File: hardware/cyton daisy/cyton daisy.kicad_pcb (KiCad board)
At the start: 4 copper layers, 61.4 x 39.7 mm, 41 parts, among them J1 Conn_02x13_Odd_Even, J2 Conn_01x08, J4 Conn_01x02, U1 ADS129x

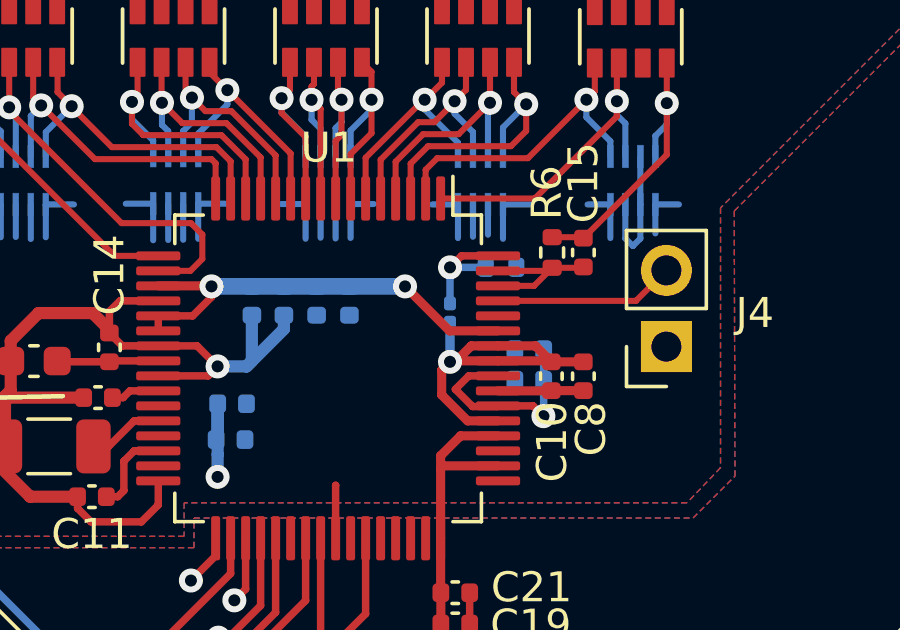
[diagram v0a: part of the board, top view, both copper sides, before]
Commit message: changed C27 from an 0402 package to a 0201 package
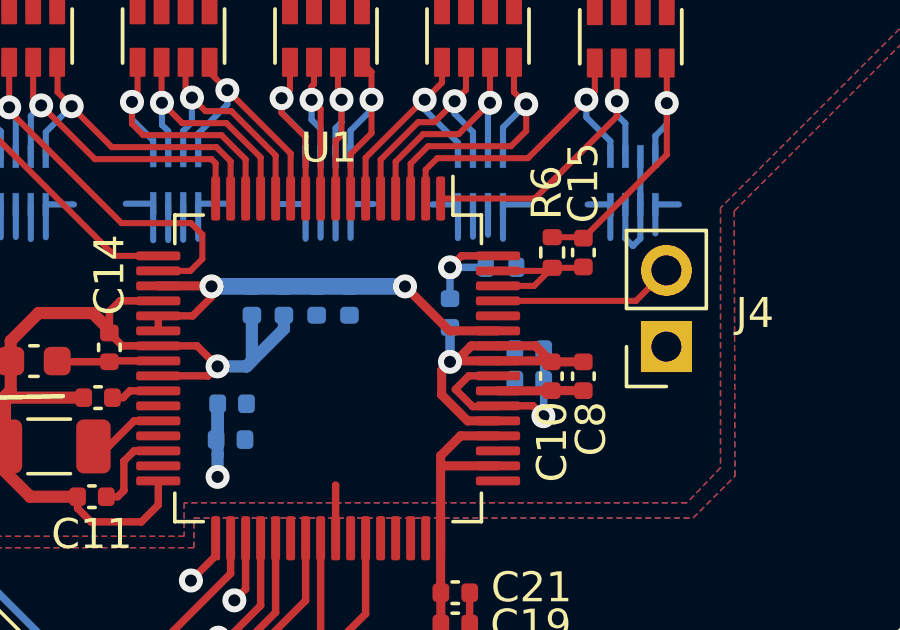
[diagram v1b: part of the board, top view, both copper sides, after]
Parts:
- C27: footprint Capacitor_SMD:C_0201_0603Metric -> Capacitor_SMD:C_0402_1005Metric
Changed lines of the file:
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@@
     )
   )
-  (footprint "Capacitor_SMD:C_0201_0603Metric" (layer "B.Cu")
+  (footprint "Capacitor_SMD:C_0402_1005Metric" (layer "B.Cu")
     (at 142.6972 100.0252 90)
-    (descr "Capacitor SMD 0201 (0603 Metric), square (rectangular) end terminal, IPC_7351 nominal, (Body size source: https://www.vishay.com/docs/20052/crcw0201e3.pdf), generated with kicad-footprint-generator")
+    (descr "Capacitor SMD 0402 (1005 Metric), square (rectangular) end terminal, IPC_7351 nominal, (Body size source: IPC-SM-782 page 76, https://www.pcb-3d.com/wordpress/wp-content/uploads/ipc-sm-782a_amendment_1_and_2.pdf), generated with kicad-footprint-generator")
     (tags "capacitor")
     (property "Sheetfile" "../shared schematics/ADS129X-X functionality.kicad_sch")
@@
     (property "ki_keywords" "cap capacitor")
     (attr smd)
-    (fp_text reference "C27" (at -2.159 0 90) (layer "B.SilkS")
-        (effects (font (size 1 1) (thickness 0.15)) (justify mirror))
-    )
-    (fp_text value "1nF" (at 0 -1.05 90) (layer "B.Fab")
-        (effects (font (size 1 1) (thickness 0.15)) (justify mirror))
-    )
-    (fp_text user "${REFERENCE}" (at 0 0.68 90) (layer "B.Fab")
+    (fp_text reference "C27" (at 0 1.16 270) (layer "B.SilkS")
+        (effects (font (size 1 1) (thickness 0.15)) (justify mirror))
+    )
+    (fp_text value "1nF" (at 0 -1.16 270) (layer "B.Fab")
+        (effects (font (size 1 1) (thickness 0.15)) (justify mirror))
+    )
+    (fp_text user "${REFERENCE}" (at 0 0 270) (layer "B.Fab")
         (effects (font (size 0.25 0.25) (thickness 0.04)) (justify mirror))
     )
-    (fp_line (start -0.7 -0.35) (end -0.7 0.35)
-      (stroke (width 0.05) (type solid)) (layer "B.CrtYd"))
-    (fp_line (start -0.7 0.35) (end 0.7 0.35)
-      (stroke (width 0.05) (type solid)) (layer "B.CrtYd"))
-    (fp_line (start 0.7 -0.35) (end -0.7 -0.35)
-      (stroke (width 0.05) (type solid)) (layer "B.CrtYd"))
-    (fp_line (start 0.7 0.35) (end 0.7 -0.35)
-      (stroke (width 0.05) (type solid)) (layer "B.CrtYd"))
-    (fp_line (start -0.3 -0.15) (end -0.3 0.15)
-      (stroke (width 0.1) (type solid)) (layer "B.Fab"))
-    (fp_line (start -0.3 0.15) (end 0.3 0.15)
-      (stroke (width 0.1) (type solid)) (layer "B.Fab"))
-    (fp_line (start 0.3 -0.15) (end -0.3 -0.15)
-      (stroke (width 0.1) (type solid)) (layer "B.Fab"))
-    (fp_line (start 0.3 0.15) (end 0.3 -0.15)
-      (stroke (width 0.1) (type solid)) (layer "B.Fab"))
-    (pad "" smd roundrect (at -0.345 0 90) (size 0.318 0.36) (layers "B.Paste") (roundrect_rratio 0.25))
-    (pad "" smd roundrect (at 0.345 0 90) (size 0.318 0.36) (layers "B.Paste") (roundrect_rratio 0.25))
-    (pad "1" smd roundrect (at -0.32 0 90) (size 0.46 0.4) (layers "B.Cu" "B.Mask") (roundrect_rratio 0.25)
+    (fp_line (start -0.107836 -0.36) (end 0.107836 -0.36)
+      (stroke (width 0.12) (type solid)) (layer "B.SilkS"))
+    (fp_line (start -0.107836 0.36) (end 0.107836 0.36)
+      (stroke (width 0.12) (type solid)) (layer "B.SilkS"))
+    (fp_line (start -0.91 -0.46) (end -0.91 0.46)
+      (stroke (width 0.05) (type solid)) (layer "B.CrtYd"))
+    (fp_line (start -0.91 0.46) (end 0.91 0.46)
+      (stroke (width 0.05) (type solid)) (layer "B.CrtYd"))
+    (fp_line (start 0.91 -0.46) (end -0.91 -0.46)
+      (stroke (width 0.05) (type solid)) (layer "B.CrtYd"))
+    (fp_line (start 0.91 0.46) (end 0.91 -0.46)
+      (stroke (width 0.05) (type solid)) (layer "B.CrtYd"))
+    (fp_line (start -0.5 -0.25) (end -0.5 0.25)
+      (stroke (width 0.1) (type solid)) (layer "B.Fab"))
+    (fp_line (start -0.5 0.25) (end 0.5 0.25)
+      (stroke (width 0.1) (type solid)) (layer "B.Fab"))
+    (fp_line (start 0.5 -0.25) (end -0.5 -0.25)
+      (stroke (width 0.1) (type solid)) (layer "B.Fab"))
+    (fp_line (start 0.5 0.25) (end 0.5 -0.25)
+      (stroke (width 0.1) (type solid)) (layer "B.Fab"))
+    (pad "1" smd roundrect (at -0.48 0 90) (size 0.56 0.62) (layers "B.Cu" "B.Paste" "B.Mask") (roundrect_rratio 0.25)
       (net 21 "VSSA") (pintype "passive"))
-    (pad "2" smd roundrect (at 0.32 0 90) (size 0.46 0.4) (layers "B.Cu" "B.Mask") (roundrect_rratio 0.25)
+    (pad "2" smd roundrect (at 0.48 0 90) (size 0.56 0.62) (layers "B.Cu" "B.Paste" "B.Mask") (roundrect_rratio 0.25)
       (net 31 "Net-(U1-WCT)") (pintype "passive"))
-    (model "${KICAD6_3DMODEL_DIR}/Capacitor_SMD.3dshapes/C_0201_0603Metric.wrl"
+    (model "${KICAD6_3DMODEL_DIR}/Capacitor_SMD.3dshapes/C_0402_1005Metric.wrl"
       (offset (xyz 0 0 0))
       (scale (xyz 1 1 1))
@@
   (via (at 134.9502 105.4862) (size 0.8) (drill 0.4) (layers "F.Cu" "B.Cu") (free) (net 21))
   (via (at 142.6972 101.6508) (size 0.8) (drill 0.4) (layers "F.Cu" "B.Cu") (net 21))
+  (segment (start 142.6972 101.6508) (end 142.6972 100.5052) (width 0.3048) (layer "B.Cu") (net 21))
   (segment (start 134.9502 105.4862) (end 134.9502 104.7424) (width 0.4064) (layer "B.Cu") (net 21))
   (segment (start 135.9154 101.8032) (end 137.16 100.5586) (width 0.4064) (layer "B.Cu") (net 21))
@@
   (segment (start 124.6632 87.63) (end 126.176799 89.143599) (width 0.2032) (layer "B.Cu") (net 21))
   (segment (start 134.9528 103.0478) (end 134.9528 104.1934) (width 0.4064) (layer "B.Cu") (net 21))
-  (segment (start 142.6972 101.6508) (end 142.6972 100.3452) (width 0.3048) (layer "B.Cu") (net 21))
   (segment (start 132.0264 102.6188) (end 132.9724 102.6188) (width 0.25) (layer "F.Cu") (net 22))
   (segment (start 131.8006 102.8446) (end 132.0264 102.6188) (width 0.25) (layer "F.Cu") (net 22))
@@
   (segment (start 143.0796 98.1188) (end 144.2974 98.1188) (width 0.25) (layer "F.Cu") (net 31))
   (via (at 142.6972 98.5012) (size 0.8) (drill 0.4) (layers "F.Cu" "B.Cu") (net 31))
+  (segment (start 142.6972 99.5452) (end 142.6972 98.5012) (width 0.25) (layer "B.Cu") (net 31))
   (segment (start 142.6972 98.5012) (end 143.889 98.5012) (width 0.25) (layer "B.Cu") (net 31))
-  (segment (start 142.6972 99.7052) (end 142.6972 98.5012) (width 0.25) (layer "B.Cu") (net 31))
   (segment (start 129.7432 84.9884) (end 129.7432 86.5886) (width 0.2032) (layer "F.Cu") (net 32))
   (segment (start 128.8032 87.5286) (end 128.8032 89.916) (width 0.2032) (layer "F.Cu") (net 32))

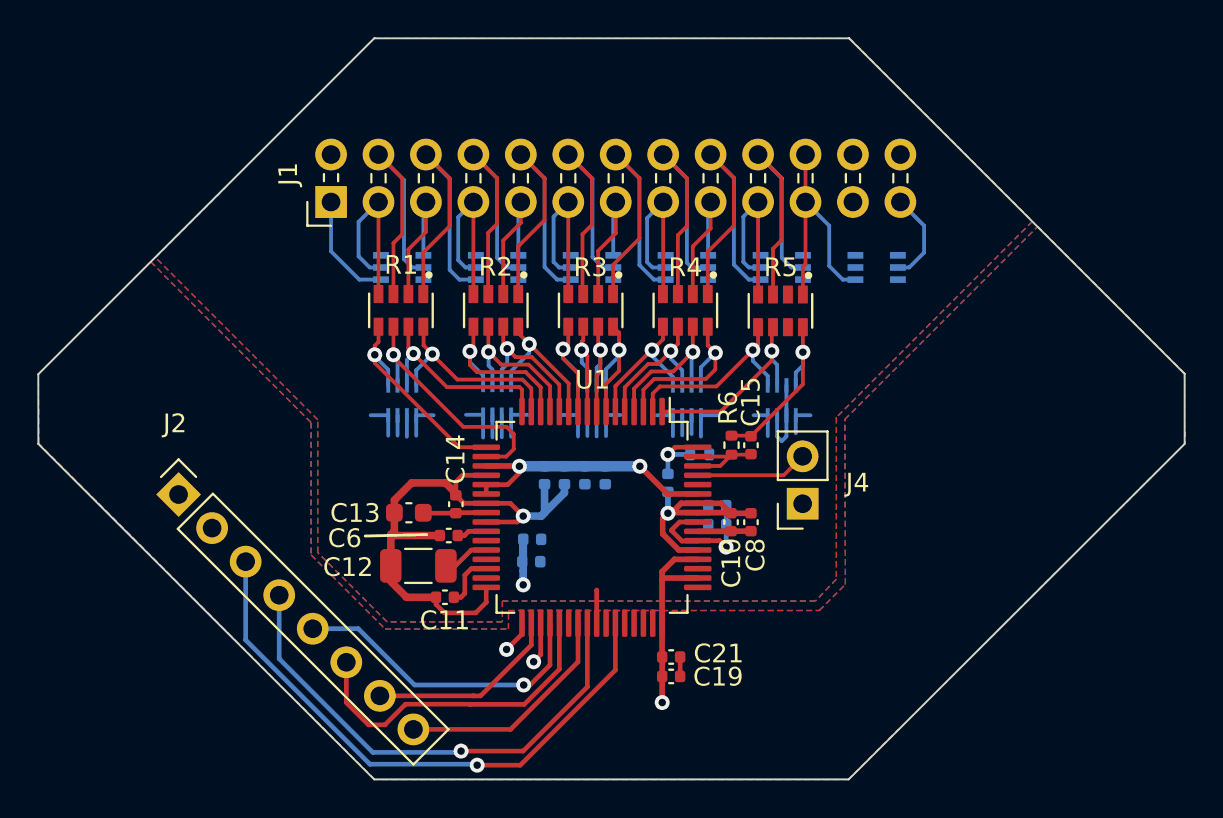
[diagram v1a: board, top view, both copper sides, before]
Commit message: changed C27 from an 0402 package to a 0201 package
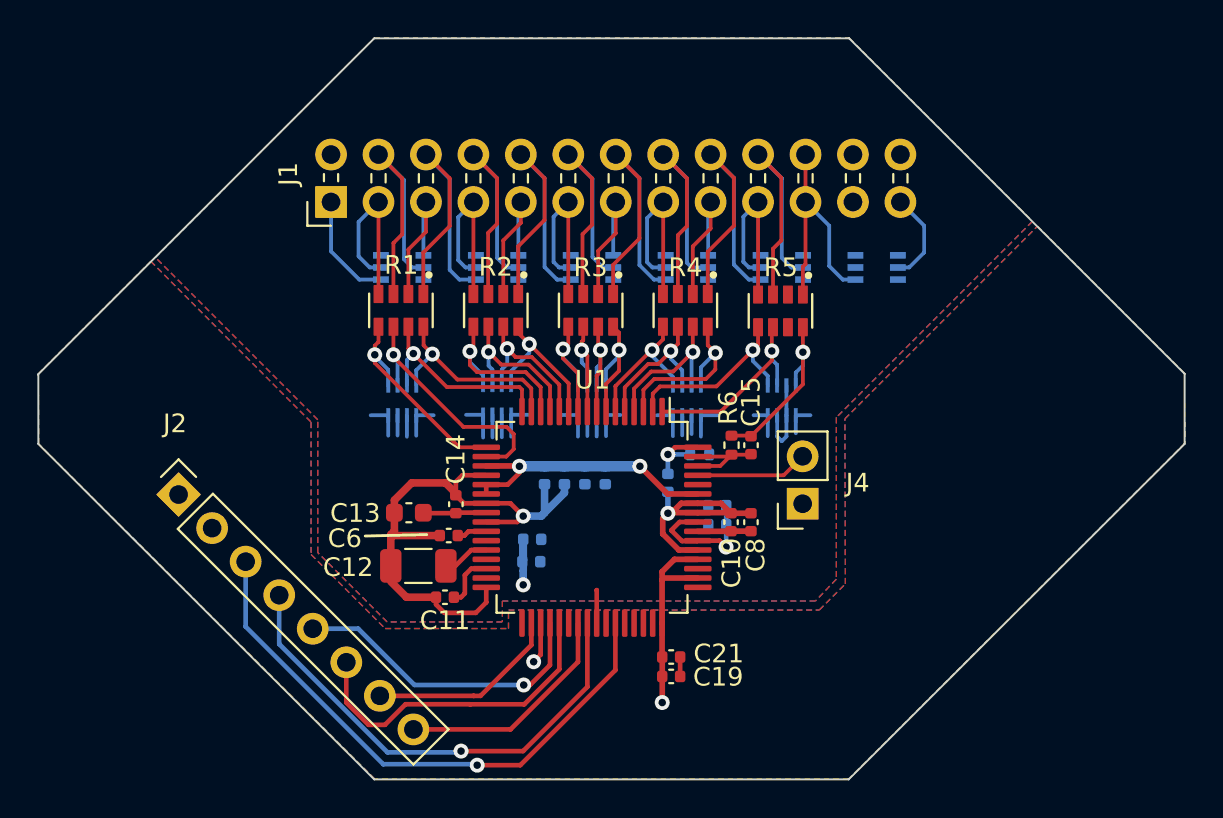
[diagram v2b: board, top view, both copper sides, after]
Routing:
- net GNDA: track 38.0 -> 36.2 mm, vias 1 -> 0
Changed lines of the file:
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@@
   (segment (start 138.8849 105.7679) (end 138.8872 105.7656) (width 0.25) (layer "F.Cu") (net 1))
   (segment (start 143.3524 109.347) (end 143.3524 110.3884) (width 0.25) (layer "F.Cu") (net 1))
-  (segment (start 134.8849 108.1169) (end 134.0612 108.9406) (width 0.25) (layer "F.Cu") (net 1))
-  (segment (start 134.8849 107.5313) (end 134.8849 108.1169) (width 0.25) (layer "F.Cu") (net 1))
   (segment (start 143.3545 109.3491) (end 143.3524 109.347) (width 0.25) (layer "F.Cu") (net 1))
-  (via (at 134.0612 108.9406) (size 0.8) (drill 0.4) (layers "F.Cu" "B.Cu") (net 1))
   (segment (start 137.8832 96.3913) (end 137.8832 97.548) (width 0.2032) (layer "B.Cu") (net 1))
   (segment (start 139.3832 96.3913) (end 140.1555 96.3913) (width 0.2032) (layer "B.Cu") (net 1))
@@
   (segment (start 138.3849 110.9461) (end 138.3849 107.5313) (width 0.25) (layer "F.Cu") (net 50))
   (via (at 131.6228 114.3851) (size 0.8) (drill 0.4) (layers "F.Cu" "B.Cu") (net 50))
-  (segment (start 126.8984 114.4524) (end 121.888154 109.442154) (width 0.25) (layer "B.Cu") (net 50))
-  (segment (start 121.888154 109.442154) (end 121.888154 106.038154) (width 0.25) (layer "B.Cu") (net 50))
-  (segment (start 131.5555 114.4524) (end 126.8984 114.4524) (width 0.25) (layer "B.Cu") (net 50))
   (segment (start 131.6228 114.3851) (end 131.5555 114.4524) (width 0.25) (layer "B.Cu") (net 50))
+  (segment (start 131.5555 114.4524) (end 127.6858 114.4524) (width 0.25) (layer "B.Cu") (net 50))
+  (segment (start 121.888154 108.654754) (end 121.888154 106.038154) (width 0.25) (layer "B.Cu") (net 50))
+  (segment (start 127.6858 114.4524) (end 121.888154 108.654754) (width 0.25) (layer "B.Cu") (net 50))
   (segment (start 135.315105 110.8456) (end 136.3849 109.775805) (width 0.25) (layer "F.Cu") (net 51))
   (segment (start 134.9756 110.8456) (end 135.315105 110.8456) (width 0.25) (layer "F.Cu") (net 51))
@@
   (segment (start 132.4864 115.1382) (end 134.7978 115.1382) (width 0.25) (layer "F.Cu") (net 56))
   (via (at 132.4864 115.1382) (size 0.8) (drill 0.4) (layers "F.Cu" "B.Cu") (net 56))
-  (segment (start 126.746 115.0874) (end 120.092102 108.433502) (width 0.25) (layer "B.Cu") (net 56))
-  (segment (start 132.4356 115.0874) (end 126.746 115.0874) (width 0.25) (layer "B.Cu") (net 56))
   (segment (start 132.4864 115.1382) (end 132.4356 115.0874) (width 0.25) (layer "B.Cu") (net 56))
-  (segment (start 120.092102 108.433502) (end 120.092102 104.242102) (width 0.25) (layer "B.Cu") (net 56))
+  (segment (start 127.4572 115.0874) (end 120.092102 107.722302) (width 0.25) (layer "B.Cu") (net 56))
+  (segment (start 132.4356 115.0874) (end 127.4572 115.0874) (width 0.25) (layer "B.Cu") (net 56))
+  (segment (start 120.092102 107.722302) (end 120.092102 104.242102) (width 0.25) (layer "B.Cu") (net 56))
   (segment (start 127.2032 84.9884) (end 127.2032 89.916) (width 0.2032) (layer "F.Cu") (net 64))
   (segment (start 126.1364 86.0552) (end 127.2032 84.9884) (width 0.2032) (layer "B.Cu") (net 64))
@@
     (polygon
       (pts
-        (xy 170.3578 94.1832)
-        (xy 170.3832 97.917)
-        (xy 152.3746 115.9002)
-        (xy 127 115.9002)
-        (xy 109.0168 97.917)
-        (xy 108.9914 94.2086)
-        (xy 115.0112 88.1888)
-        (xy 123.5964 96.7994)
-        (xy 123.5964 103.886)
-        (xy 127.5588 107.8484)
-        (xy 134.1628 107.8484)
-        (xy 134.1628 106.8578)
-        (xy 150.7998 106.8578)
-        (xy 152.1968 105.4608)
-        (xy 152.1714 96.6216)
-        (xy 162.4838 86.3092)
+        (xy 170.3578 94.1578)
+        (xy 170.3832 97.8916)
+        (xy 152.3746 115.8748)
+        (xy 127 115.8748)
+        (xy 109.0168 97.9424)
+        (xy 108.9914 94.1832)
+        (xy 115.0112 88.1634)
+        (xy 123.5964 96.774)
+        (xy 123.5964 103.8606)
+        (xy 127.5588 107.823)
+        (xy 134.1628 107.823)
+        (xy 134.1628 106.8324)
+        (xy 150.7998 106.8324)
+        (xy 152.1968 105.4354)
+        (xy 152.1714 96.5962)
+        (xy 162.4838 86.2838)
       )
     )
